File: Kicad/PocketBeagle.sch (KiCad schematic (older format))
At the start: 2 parts, among them U1 POCKETBEAGLE-SC-569

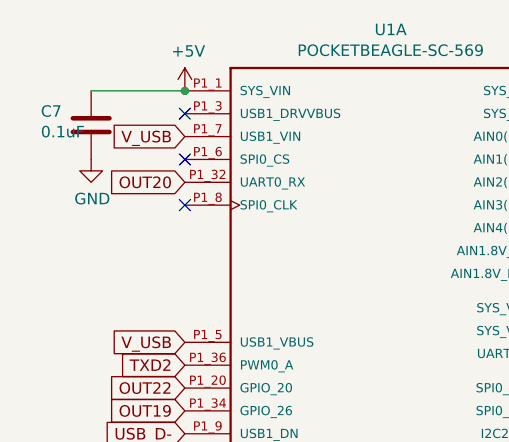
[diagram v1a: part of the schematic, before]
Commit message: Added LOR/DMX Serial Port Selector, EEPROM, and Push buttons
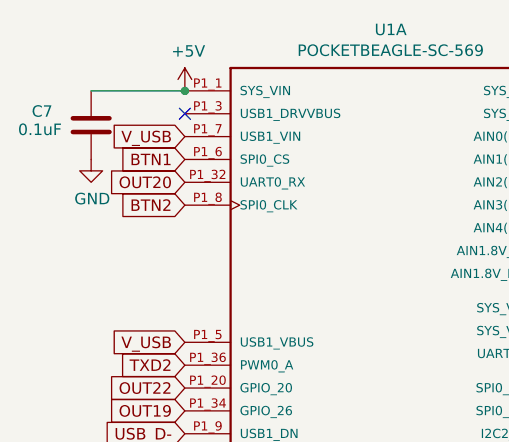
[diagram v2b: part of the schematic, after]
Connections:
- net BTN1: now reaches U1.P1_6 (SPI0_CS)
- net BTN2: now reaches U1.P1_8 (SPI0_CLK)
- no-connect marks 21 -> 19
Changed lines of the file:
@@
 Sheet 2 5
 Title "PB 16"
-Date "2019-09-19"
-Rev "v1.0e"
+Date "2019-10-07"
+Rev "v1.0f"
 Comp "Scott Hanson"
 Comment1 ""
@@
 NoConn ~ 5270 3090
 NoConn ~ 3470 2590
-NoConn ~ 3470 2790
-NoConn ~ 3470 2990
 NoConn ~ 6820 2740
 NoConn ~ 8620 2740
@@
 U 1 1 5D540524
 P 3060 2640
-F 0 "C7" H 2840 2700 50  0000 L CNN
-F 1 "0.1uF" H 2840 2610 50  0000 L CNN
+F 0 "C7" H 2800 2700 50  0000 L CNN
+F 1 "0.1uF" H 2740 2620 50  0000 L CNN
 F 2 "Capacitor_THT:C_Rect_L7.0mm_W2.0mm_P5.00mm" H 3098 2490 50  0001 C CNN
 F 3 "~" H 3060 2640 50  0001 C CNN
@@
 Text GLabel 5270 4290 2    50   Input ~ 0
 GPIO2
+Text GLabel 3470 2990 0    50   Input ~ 0
+BTN2
+Text GLabel 3470 2790 0    50   Input ~ 0
+BTN1
 $EndSCHEMATC

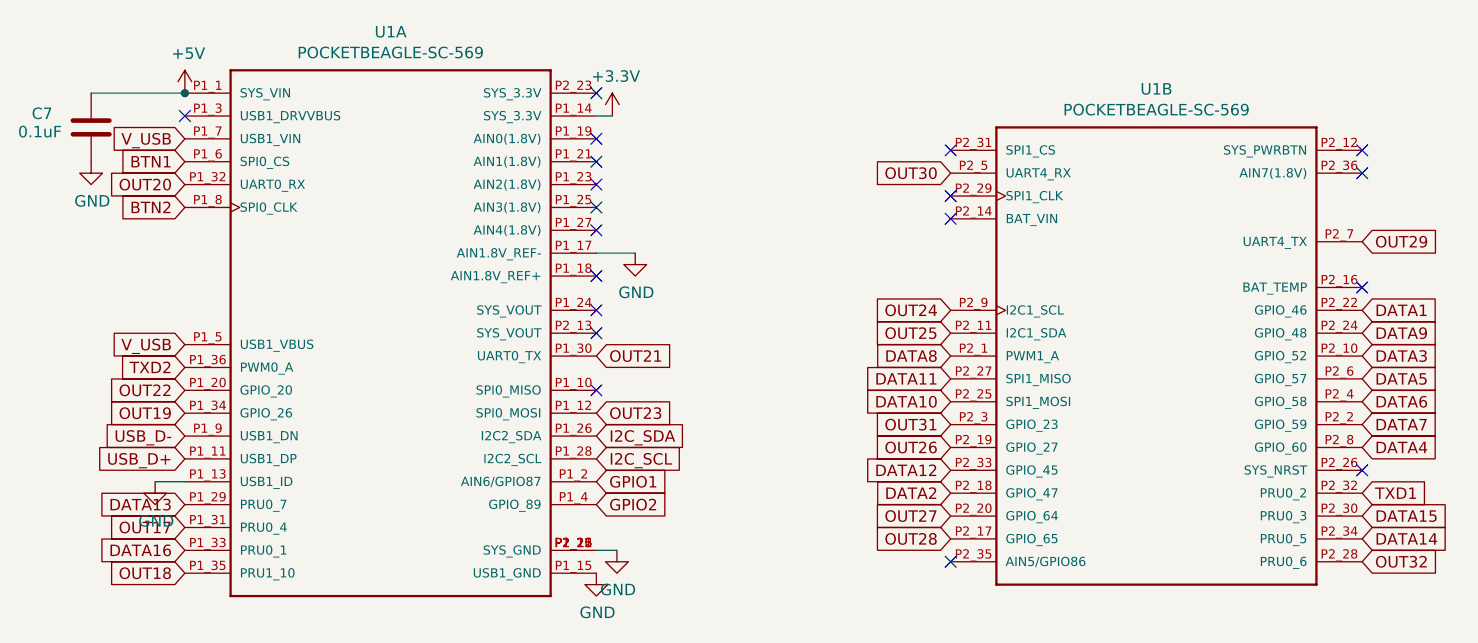
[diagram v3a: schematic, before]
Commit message: cleaning up schematic
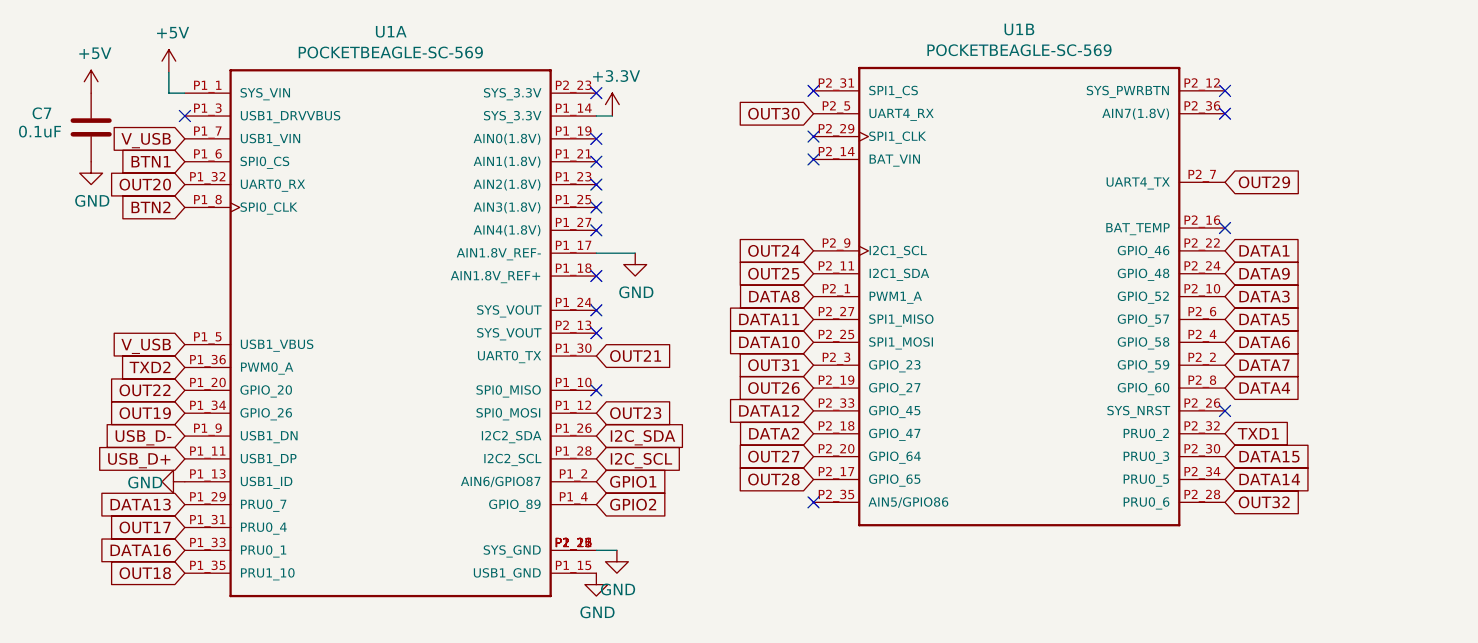
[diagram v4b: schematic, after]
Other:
- moved on the sheet: U1B
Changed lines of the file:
@@
 L POCKETBEAGLE:POCKETBEAGLE-SC-569 U1
 U 2 1 5D4189E5
-P 7720 3640
-F 0 "U1" H 7720 4807 50  0000 C CNN
-F 1 "POCKETBEAGLE-SC-569" H 7720 4716 50  0000 C CNN
-F 2 "POCKETBEAGLE:BEAGLE_POCKETBEAGLE-SC-569" H 7720 3640 50  0001 L BNN
-F 3 "" H 7720 3640 50  0001 L BNN
-F 4 "https://www.digikey.com/product-detail/en/ghi-electronics-llc/POCKETBEAGLE-SC-569/POCKETBEAGLE-SC-569-ND/7603326?utm_source=snapeda&utm_medium=aggregator&utm_campaign=symbol" H 7720 3640 50  0001 L BNN "Field4"
-F 5 "POCKETBEAGLE-SC-569" H 7720 3640 50  0001 L BNN "Field5"
-F 6 "None" H 7720 3640 50  0001 L BNN "Field6"
-F 7 "POCKETBEAGLE-SC-569-ND" H 7720 3640 50  0001 L BNN "Field7"
-F 8 "GHI Electronics," H 7720 3640 50  0001 L BNN "Field8"
-F 9 "POCKETBEAGLE-SC-569-ND" H 7720 3640 50  0001 C CNN "Digi-Key_PN"
-F 10 "POCKETBEAGLE-SC-569" H 7720 3640 50  0001 C CNN "MPN"
-	2    7720 3640
+P 7120 3380
+F 0 "U1" H 7120 4547 50  0000 C CNN
+F 1 "POCKETBEAGLE-SC-569" H 7120 4456 50  0000 C CNN
+F 2 "POCKETBEAGLE:BEAGLE_POCKETBEAGLE-SC-569" H 7120 3380 50  0001 L BNN
+F 3 "" H 7120 3380 50  0001 L BNN
+F 4 "https://www.digikey.com/product-detail/en/ghi-electronics-llc/POCKETBEAGLE-SC-569/POCKETBEAGLE-SC-569-ND/7603326?utm_source=snapeda&utm_medium=aggregator&utm_campaign=symbol" H 7120 3380 50  0001 L BNN "Field4"
+F 5 "POCKETBEAGLE-SC-569" H 7120 3380 50  0001 L BNN "Field5"
+F 6 "None" H 7120 3380 50  0001 L BNN "Field6"
+F 7 "POCKETBEAGLE-SC-569-ND" H 7120 3380 50  0001 L BNN "Field7"
+F 8 "GHI Electronics," H 7120 3380 50  0001 L BNN "Field8"
+F 9 "POCKETBEAGLE-SC-569-ND" H 7120 3380 50  0001 C CNN "Digi-Key_PN"
+F 10 "POCKETBEAGLE-SC-569" H 7120 3380 50  0001 C CNN "MPN"
+	2    7120 3380
 	1    0    0    -1
 $EndComp
@@
 L power:+5V #PWR05
 U 1 1 5D542B82
-P 3470 2490
-F 0 "#PWR05" H 3470 2340 50  0001 C CNN
-F 1 "+5V" H 3485 2663 50  0000 C CNN
-F 2 "" H 3470 2490 50  0001 C CNN
-F 3 "" H 3470 2490 50  0001 C CNN
-	1    3470 2490
+P 3400 2400
+F 0 "#PWR05" H 3400 2250 50  0001 C CNN
+F 1 "+5V" H 3415 2573 50  0000 C CNN
+F 2 "" H 3400 2400 50  0001 C CNN
+F 3 "" H 3400 2400 50  0001 C CNN
+	1    3400 2400
 	1    0    0    -1
 $EndComp
@@
 	1    0    0    -1
 $EndComp
-Wire Wire Line
-	3470 4190 3340 4190
 Text GLabel 3470 3990 0    50   Input ~ 0
 USB_D-
@@
 Wire Wire Line
 	5270 4490 5360 4490
-Text GLabel 8620 3940 2    50   Input ~ 0
+Text GLabel 8020 3680 2    50   Input ~ 0
 DATA7
-Text GLabel 8620 3840 2    50   Input ~ 0
+Text GLabel 8020 3580 2    50   Input ~ 0
 DATA6
-Text GLabel 8620 3740 2    50   Input ~ 0
+Text GLabel 8020 3480 2    50   Input ~ 0
 DATA5
-Text GLabel 8620 4040 2    50   Input ~ 0
+Text GLabel 8020 3780 2    50   Input ~ 0
 DATA4
-Text GLabel 8620 3640 2    50   Input ~ 0
+Text GLabel 8020 3380 2    50   Input ~ 0
 DATA3
-Text GLabel 6820 4240 0    50   Input ~ 0
+Text GLabel 6220 3980 0    50   Input ~ 0
 DATA2
-Text GLabel 8620 3440 2    50   Input ~ 0
+Text GLabel 8020 3180 2    50   Input ~ 0
 DATA1
 Text GLabel 3470 4490 0    50   Input ~ 0
 DATA16
-Text GLabel 8620 4340 2    50   Input ~ 0
+Text GLabel 8020 4080 2    50   Input ~ 0
 DATA15
-Text GLabel 8620 4440 2    50   Input ~ 0
+Text GLabel 8020 4180 2    50   Input ~ 0
 DATA14
 Text GLabel 3470 4290 0    50   Input ~ 0
 DATA13
-Text GLabel 6820 4140 0    50   Input ~ 0
+Text GLabel 6220 3880 0    50   Input ~ 0
 DATA12
-Text GLabel 6820 3740 0    50   Input ~ 0
+Text GLabel 6220 3480 0    50   Input ~ 0
 DATA11
-Text GLabel 6820 3840 0    50   Input ~ 0
+Text GLabel 6220 3580 0    50   Input ~ 0
 DATA10
-Text GLabel 8620 3540 2    50   Input ~ 0
+Text GLabel 8020 3280 2    50   Input ~ 0
 DATA9
-Text GLabel 8620 4240 2    50   Input ~ 0
+Text GLabel 8020 3980 2    50   Input ~ 0
 TXD1
 Text GLabel 3470 3690 0    50   Input ~ 0
 TXD2
-Text GLabel 6820 4040 0    50   Input ~ 0
+Text GLabel 6220 3780 0    50   Input ~ 0
 OUT26
-Text GLabel 6820 4340 0    50   Input ~ 0
+Text GLabel 6220 4080 0    50   Input ~ 0
 OUT27
-Text GLabel 6820 4440 0    50   Input ~ 0
+Text GLabel 6220 4180 0    50   Input ~ 0
 OUT28
-Text GLabel 8620 3140 2    50   Input ~ 0
+Text GLabel 8020 2880 2    50   Input ~ 0
 OUT29
-Text GLabel 6820 2840 0    50   Input ~ 0
+Text GLabel 6220 2580 0    50   Input ~ 0
 OUT30
-Text GLabel 6820 3940 0    50   Input ~ 0
+Text GLabel 6220 3680 0    50   Input ~ 0
 OUT31
 Text GLabel 3470 4590 0    50   Input ~ 0
@@
 Text GLabel 5270 3890 2    50   Input ~ 0
 OUT23
-Text GLabel 6820 3540 0    50   Input ~ 0
+Text GLabel 6220 3280 0    50   Input ~ 0
 OUT25
 Wire Wire Line
@@
 NoConn ~ 5270 3090
 NoConn ~ 3470 2590
-NoConn ~ 6820 2740
-NoConn ~ 8620 2740
-NoConn ~ 8620 2840
-NoConn ~ 8620 3340
-NoConn ~ 8620 4140
-NoConn ~ 6820 4540
-NoConn ~ 6820 3040
+NoConn ~ 6220 2480
+NoConn ~ 8020 2480
+NoConn ~ 8020 2580
+NoConn ~ 8020 3080
+NoConn ~ 8020 3880
+NoConn ~ 6220 4280
+NoConn ~ 6220 2780
 NoConn ~ 5270 2490
 $Comp
@@
 Wire Wire Line
 	5270 3190 5440 3190
-Text GLabel 6820 3440 0    50   Input ~ 0
+Text GLabel 6220 3180 0    50   Input ~ 0
 OUT24
 Text GLabel 3470 3890 0    50   Input ~ 0
@@
 Text GLabel 3470 2890 0    50   Input ~ 0
 OUT20
-Text GLabel 8620 4540 2    50   Input ~ 0
+Text GLabel 8020 4280 2    50   Input ~ 0
 OUT32
 $Comp
 L power:GND #PWR04
 U 1 1 5D545435
-P 3340 4190
-F 0 "#PWR04" H 3340 3940 50  0001 C CNN
-F 1 "GND" H 3345 4017 50  0000 C CNN
-F 2 "" H 3340 4190 50  0001 C CNN
-F 3 "" H 3340 4190 50  0001 C CNN
-	1    3340 4190
-	1    0    0    -1
+P 3470 4190
+F 0 "#PWR04" H 3470 3940 50  0001 C CNN
+F 1 "GND" V 3475 4017 50  0000 C CNN
+F 2 "" H 3470 4190 50  0001 C CNN
+F 3 "" H 3470 4190 50  0001 C CNN
+	1    3470 4190
+	0    1    1    0
 $EndComp
 Text GLabel 3470 4390 0    50   Input ~ 0
 OUT17
-Wire Wire Line
-	3060 2490 3470 2490
-Connection ~ 3470 2490
 $Comp
 L Device:C C7
@@
 Text GLabel 5270 3990 2    50   Input ~ 0
 I2C_SDA
-Text GLabel 6820 3640 0    50   Input ~ 0
+Text GLabel 6220 3380 0    50   Input ~ 0
 DATA8
-NoConn ~ 6820 2940
+NoConn ~ 6220 2680
 Text GLabel 5270 4190 2    50   Input ~ 0
 GPIO1
@@
 Text GLabel 3470 2790 0    50   Input ~ 0
 BTN1
+$Comp
+L power:+5V #PWR?
+U 1 1 5ECC089C
+P 3060 2490
+F 0 "#PWR?" H 3060 2340 50  0001 C CNN
+F 1 "+5V" H 3075 2663 50  0000 C CNN
+F 2 "" H 3060 2490 50  0001 C CNN
+F 3 "" H 3060 2490 50  0001 C CNN
+	1    3060 2490
+	1    0    0    -1
+$EndComp
+Wire Wire Line
+	3470 2490 3400 2490
+Wire Wire Line
+	3400 2490 3400 2400
 $EndSCHEMATC
